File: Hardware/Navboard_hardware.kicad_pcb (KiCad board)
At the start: 2 copper layers, 68 parts, among them U1 OKI-5V, U2 OKI-3V, U3 NEO-M8P-2, U4 BNO055, U5 BMX160, U6 ICM-20948, U7 Raspberry_Pi

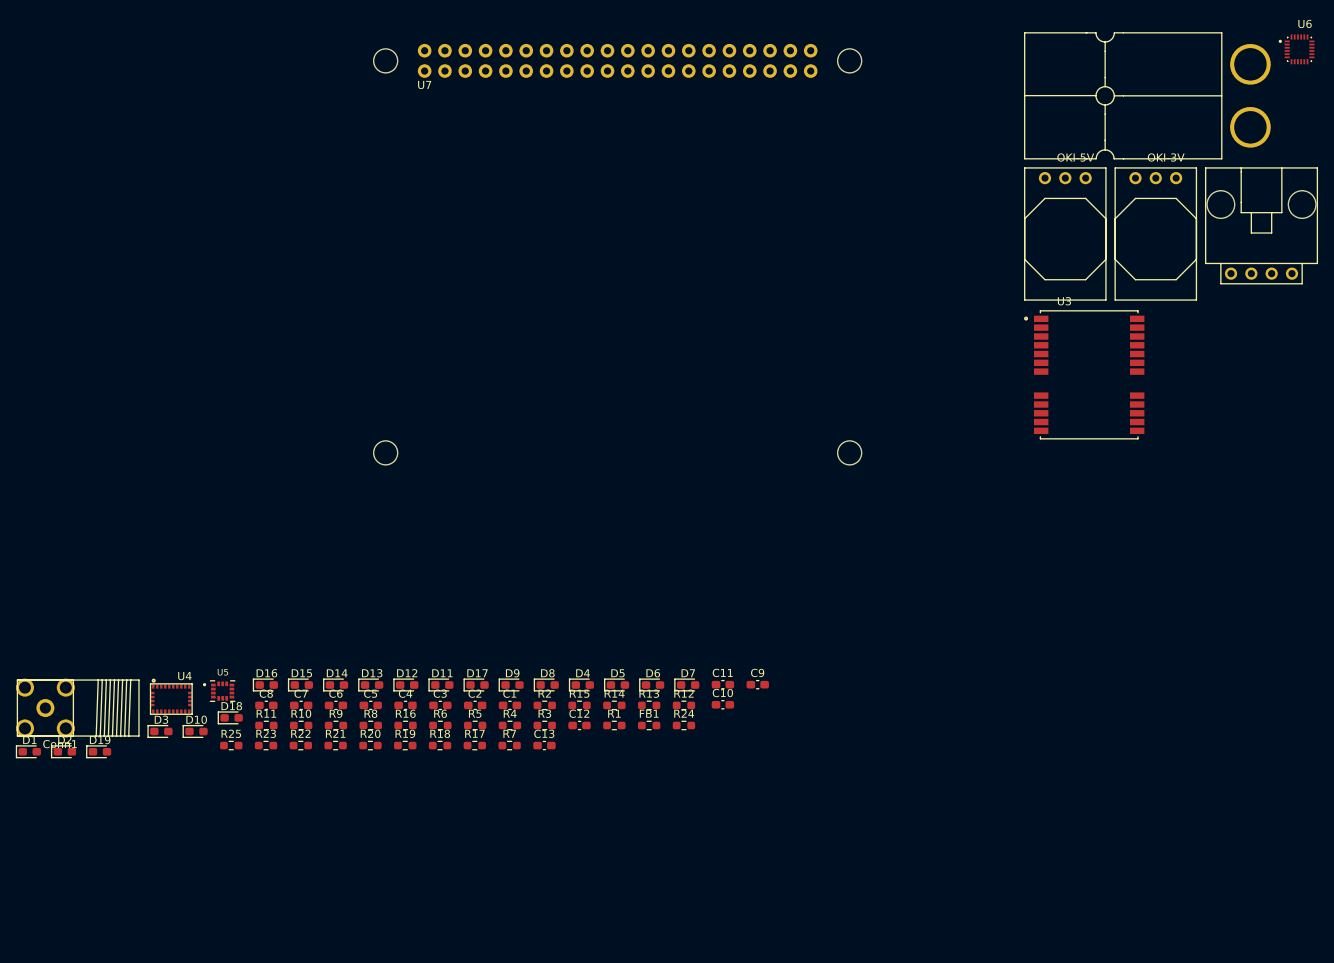
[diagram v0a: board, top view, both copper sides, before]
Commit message: Layout almost finished just need to complete LED traces.
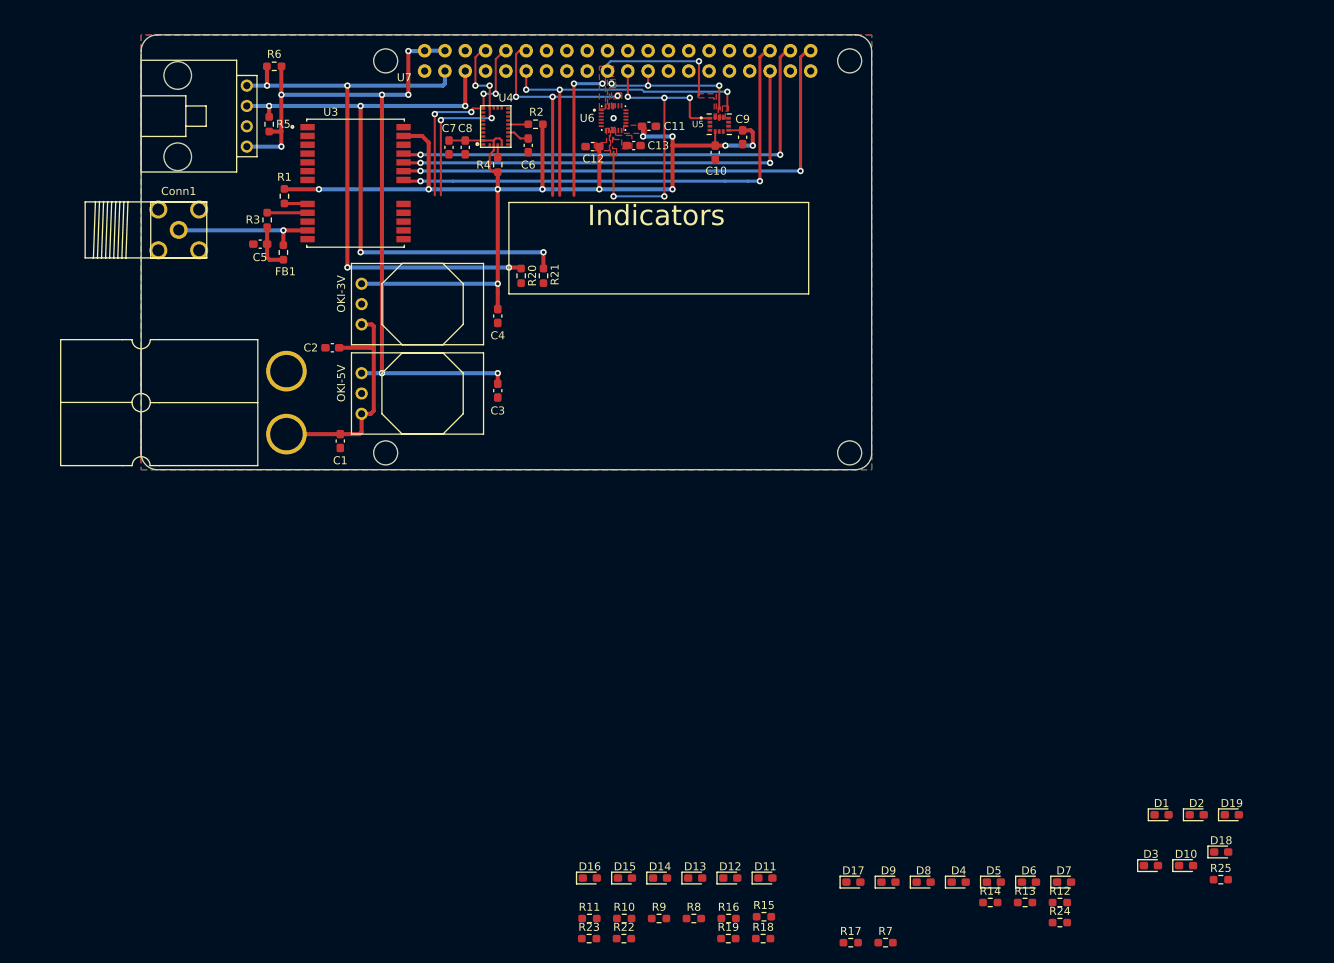
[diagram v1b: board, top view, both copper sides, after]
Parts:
- moved D1 141.7 mm to (221.7, 135.1)
- moved D19 141.7 mm to (230.4, 135.1)
- moved D2 141.7 mm to (226.1, 135.1)
- moved Conn3 126.5 mm to (112.2, 79.6)
- moved D10 124.8 mm to (224.7, 141.4)
- moved R25 124.8 mm to (229.1, 143.2)
- moved D18 124.8 mm to (229.1, 139.7)
- moved D3 124.8 mm to (220.3, 141.4)
- moved Conn2 124.0 mm to (107.3, 51.6), turned to 90 degrees
- moved U2 98.4 mm to (121.7, 73.8), turned to 90 degrees
- moved U3 94.8 mm to (120.9, 56.1)
- moved U5 94.2 mm to (166.4, 48.8)
- moved U1 90.4 mm to (121.7, 85.0), turned to 90 degrees
- moved U6 86.2 mm to (153.2, 48.0)
- moved R6 85.0 mm to (110.7, 41.5), turned to 180 degrees
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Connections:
- C10 pad 1: BMX_ON -> +3V3
- C11 pad 2: BMX_ON -> +3V3
- C12 pad 2: BMX_ON -> +3V3
- C4 pad 1: BMX_ON -> +3V3
- C7 pad 2: BMX_ON -> +3V3
- C8 pad 1: BMX_ON -> +3V3
- C9 pad 2: BMX_ON -> +3V3
- Conn2 pad 3: LiDAR_SDA -> LiDAR_SCL
- Conn2 pad 4: LiDAR_SCL -> LiDAR_SDA
- R1 pad 1: BMX_ON -> +3V3
- R2 pad 1: BMX_ON -> +3V3
- R4 pad 1: BMX_ON -> +3V3
- R8 pad 1: BMX_ON -> +3V3
- U2 pad 3: BMX_ON -> +3V3
- U3 pad 23: BMX_ON -> +3V3
- U4 pad 28: BMX_ON -> +3V3
- U4 pad 3: BMX_ON -> +3V3
- U4 pad 5: BMX_ON -> +3V3
- U5 pad 5: BMX_ON -> +3V3
- U5 pad 8: BMX_ON -> +3V3
- U6 pad 13: BMX_ON -> +3V3
- U6 pad 8: BMX_ON -> +3V3
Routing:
- net +3V3: track 0.00 -> 146.1 mm, vias 0 -> 11
- net +5V: track 0.00 -> 95.0 mm, vias 0 -> 7
- net LiDAR_SCL: track 0.00 -> 76.2 mm, vias 0 -> 5
- net LiDAR_SDA: track 0.00 -> 73.4 mm, vias 0 -> 4
- net M8P_CLK: track 0.00 -> 65.5 mm, vias 0 -> 2
- net M8P_CS: track 0.00 -> 61.7 mm, vias 0 -> 2
- net M8P_MOSI: track 0.00 -> 60.9 mm, vias 0 -> 2
- net M8P_MISO: track 0.00 -> 57.3 mm, vias 0 -> 2
- net BMX_CS: track 0.00 -> 43.1 mm, vias 0 -> 3
- net BMX_MISO: track 0.00 -> 40.3 mm, vias 0 -> 5
- net BMX_MOSI: track 0.00 -> 34.3 mm, vias 0 -> 3
- net ICM_CS: track 0.00 -> 31.9 mm, vias 0 -> 3
- net +12V: track 0.00 -> 30.0 mm
- net BNO055_RX: track 0.00 -> 27.0 mm, vias 0 -> 4
- net BNO055_TX: track 0.00 -> 26.1 mm, vias 0 -> 4
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- added copper zone on F.Cu, net +3V3
- added copper zone on F.Cu, net BMX_CLK
- added copper zone on F.Cu, net BMX_CS
- added copper zone on F.Cu, net BMX_MISO
- added copper zone on F.Cu, net BMX_MOSI
- added copper zone on B.Cu, net GND
- added copper zone on F.Cu, net GND
- added copper zone on F.Cu, net ICM_CS
- added copper zone on F.Cu, net Net-(C13-Pad2)
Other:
- board outline added: 91.3 x 54.4 mm
- board text added: "Indicators"

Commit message: Finished Layout but I still need to complete the BOM and generate GERBs.
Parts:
- removed D16, D17, D18, D19: GREEN, LED_SMD:LED_0603_1608Metric_Pad1.05x0.95mm_HandSolder
- removed R22, R23, R24, R25: 330, Resistor_SMD:R_0603_1608Metric_Pad0.98x0.95mm_HandSolder
- added G***: LOGO, MRDT_Silkscreens:z_sig_Anthony_Robles_15mmx8.2mm, F.Cu at (166.4, 85.9)
- moved D3 101.4 mm to (147.2, 71.2), turned to 90 degrees
- moved R12 96.4 mm to (152.8, 67.7), turned to 270 degrees
- moved R13 92.4 mm to (155.6, 67.7), turned to 270 degrees
- moved D7 90.2 mm to (155.6, 71.2), turned to 90 degrees
- moved D6 89.2 mm to (152.8, 71.2), turned to 90 degrees
- moved D2 89.1 mm to (164.0, 71.2), turned to 90 degrees
- moved D4 85.8 mm to (150.0, 71.2), turned to 90 degrees
- moved D10 84.4 mm to (177.9, 71.2), turned to 90 degrees
- moved R17 84.0 mm to (172.3, 67.7), turned to 270 degrees
- moved R7 83.6 mm to (180.7, 67.7), turned to 270 degrees
- moved R18 83.5 mm to (161.2, 67.7), turned to 270 degrees
- moved R19 82.9 mm to (166.8, 67.7), turned to 270 degrees
- moved R11 82.6 mm to (169.5, 67.7), turned to 270 degrees
- moved R14 82.3 mm to (175.1, 67.7), turned to 270 degrees
- moved R15 81.3 mm to (158.4, 67.7), turned to 270 degrees
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- renumbered Conn1 to Antenna
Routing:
- net +5V: track 95.0 -> 157.7 mm, vias 7 -> 10
- net BMX_MOSI: track 34.3 -> 89.1 mm, vias 3 -> 9
- net BMX_MISO: track 40.3 -> 84.1 mm, vias 5 -> 11
- net BNO055_RX: track 27.0 -> 54.5 mm, vias 4 -> 6
- net BNO055_TX: track 26.1 -> 51.6 mm, vias 4 -> 6
- net BMX_CS: track 43.1 -> 61.4 mm, vias 3 -> 5
- net ICM_CS: track 31.9 -> 48.2 mm, vias 3 -> 5
- net M8P_MOSI: track 60.9 -> 76.3 mm, vias 2 -> 4
- net M8P_MISO: track 57.3 -> 70.7 mm
- net +3V3: track 146.1 -> 159.4 mm, vias 11 -> 15
- net M8P_CS: track 61.7 -> 72.6 mm, vias 2 -> 3
- net Net-(D14-Pad2): track 0.00 -> 1.75 mm
- net Net-(D9-Pad2): track 0.00 -> 1.73 mm
- net Net-(D8-Pad2): track 0.00 -> 1.73 mm
- net Net-(D7-Pad2): track 0.00 -> 1.73 mm
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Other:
- board text added: "+"
- board text added: "-"
- board text added: "3V3"
- board text added: "5V"
- board text added: "BMX_CS"
- board text added: "BMX_MISO"
- board text added: "BMX_MOSI"
- board text added: "BNO055 RX"
- board text added: "BNO055 TX"
- board text added: "ICM_CS"
- board text added: "ICM_MISO"
- board text added: "ICM_MOSI"
- board text added: "LiDAR"
- board text added: "LiDAR SCL"
- board text added: "LiDAR SDA"
- board text added: "M8P_CS"
- board text added: "M8P_MISO"
- board text added: "M8P_MOSI"
- board text added: "Nav Board Rev 1 Mars Rover Design Team Missouri S&T, 2021 Anthony Robles"
- board text added: "SCL"
- board text added: "SDA"

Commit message: Completed the board but still needs a review.
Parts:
- added G***: LOGO, Anthony's Silkscreens:W, B.Cu at (159.7, 69.8)
